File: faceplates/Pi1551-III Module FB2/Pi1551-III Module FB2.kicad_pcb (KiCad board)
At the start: 2 copper layers, 100 x 100 mm, 7 parts, among them M1 Mounting, M2 Mounting, M3 Mounting, M4 Mounting

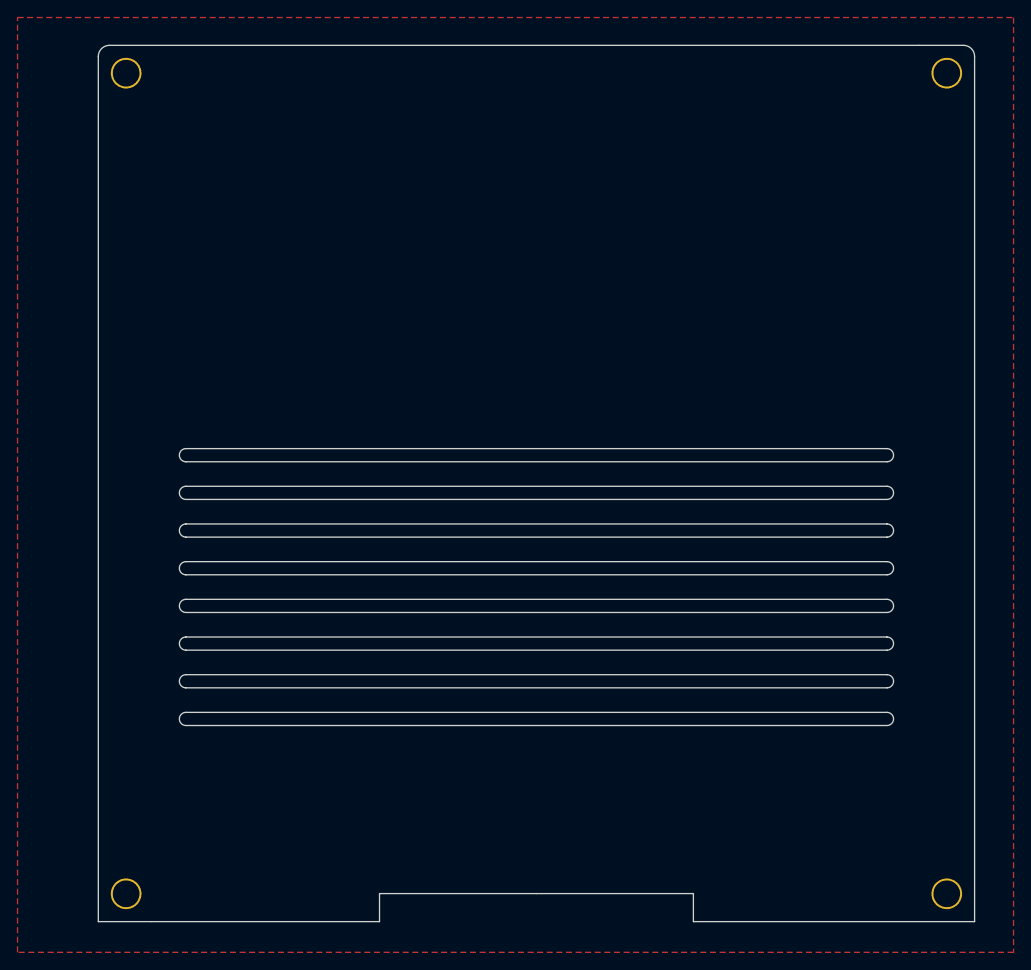
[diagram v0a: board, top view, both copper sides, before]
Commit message: upgrade to KiCad 9.0.7
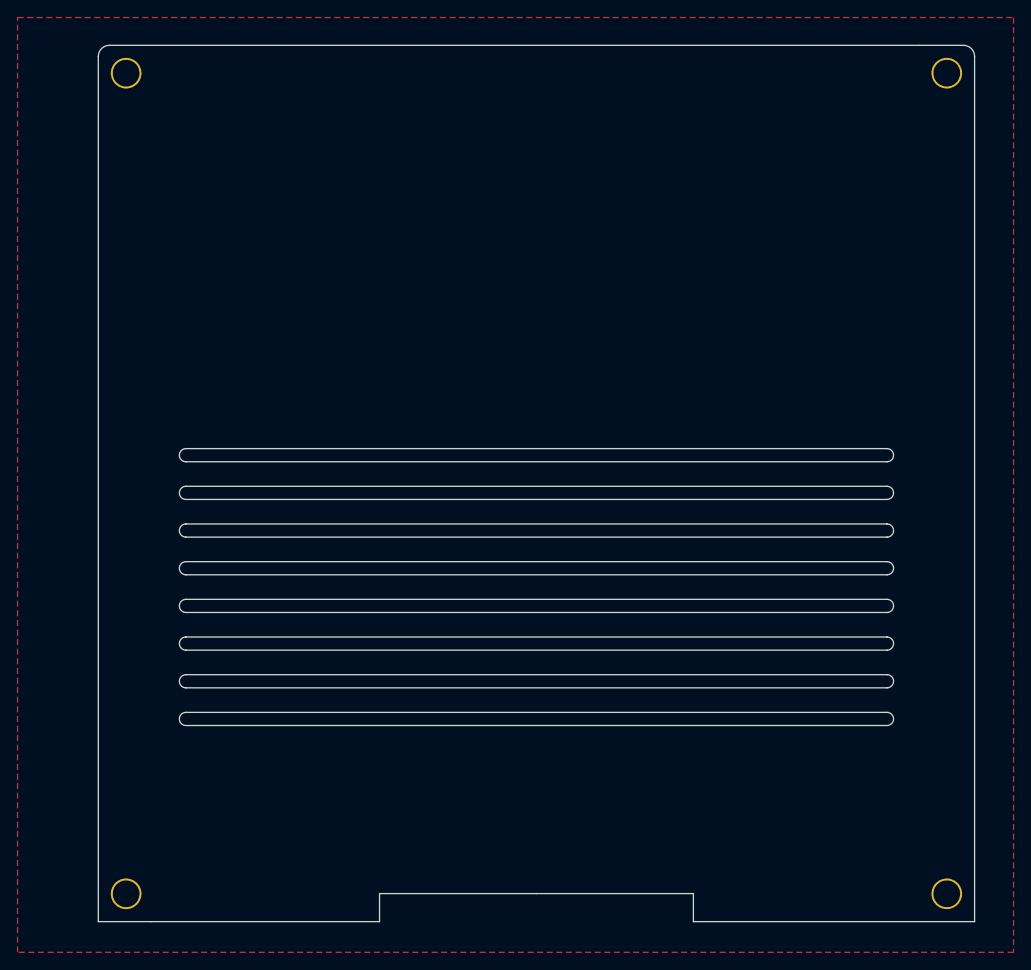
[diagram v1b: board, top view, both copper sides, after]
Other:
- net class Default removed
- net class Power removed

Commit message: PI1551 branding and Microgramma font labels
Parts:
- removed G***: LOGO, Pi1541:Pi1541-Decal2
- removed Pi1541-logo3: , Pi1541:Pi1541-logo3
- added kibuzzard-69864CDD: G***, kibuzzard-69864CDD, B.Cu at (120.0, 80.0)
- added kibuzzard-69864D02: G***, kibuzzard-69864D02, B.Cu at (120.0, 72.0)
- added kibuzzard-69864E12: G***, kibuzzard-69864E12, B.Cu at (120.2, 145.8)

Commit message: gerber files for fabrication
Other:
- board text added: "JLCJLCJLCJLC"
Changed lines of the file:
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@@
 			(disableapertmacros no)
 			(usegerberextensions yes)
-			(usegerberattributes no)
-			(usegerberadvancedattributes no)
+			(usegerberattributes yes)
+			(usegerberadvancedattributes yes)
 			(creategerberjobfile no)
 			(dashed_line_dash_ratio 12.000000)
@@
 			(drillshape 0)
 			(scaleselection 1)
-			(outputdirectory "export/")
+			(outputdirectory "gerbers/")
 		)
 	)
@@
 		(layer "Edge.Cuts")
 	)
+	(gr_text "JLCJLCJLCJLC"
+		(at 154.686 58.42 0)
+		(layer "F.SilkS")
+		(effects
+			(font
+				(size 0.8 0.8)
+				(thickness 0.15)
+			)
+			(justify left bottom)
+		)
+	)
 	(gr_text "5V DC"
